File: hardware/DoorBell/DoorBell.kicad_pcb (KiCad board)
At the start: 2 copper layers, 17.8 x 33 mm, 5 parts, among them P1 Digital, P2 COM, P3 ADC, P4 Analog, P5 ADC

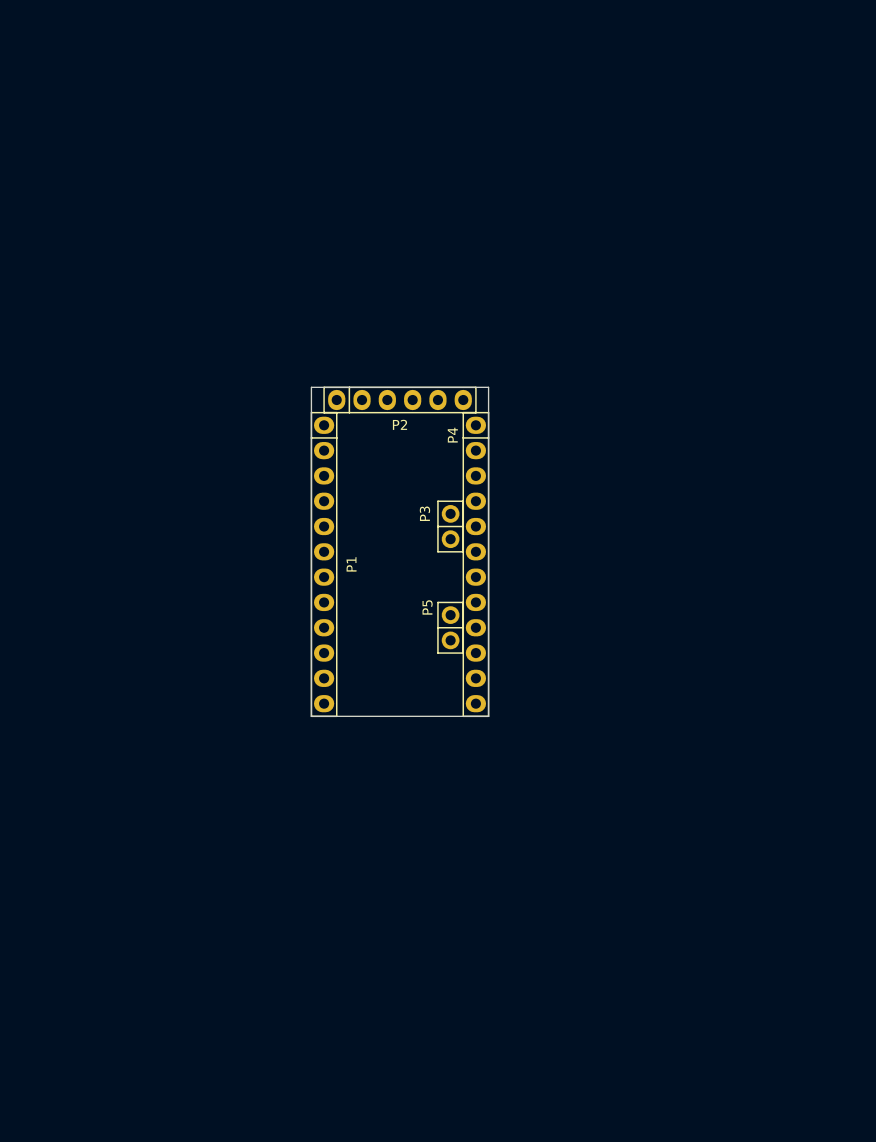
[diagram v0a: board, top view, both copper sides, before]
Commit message: Added mounting holes
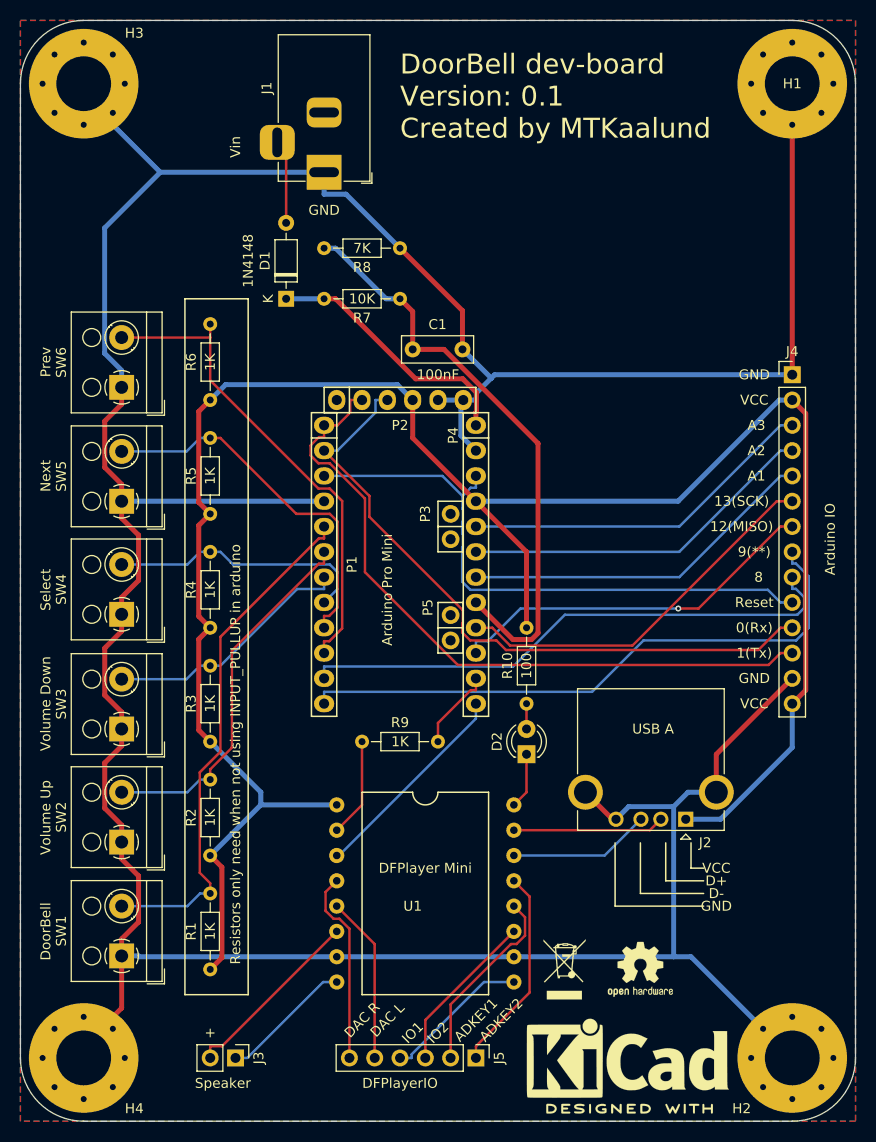
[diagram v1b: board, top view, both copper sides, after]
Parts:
- added C1: 100n, Capacitor_THT:C_Rect_L7.0mm_W2.5mm_P5.00mm, F.Cu at (147.3, 77.5)
- added D1: 1N4148, Diode_THT:D_DO-35_SOD27_P7.62mm_Horizontal, F.Cu at (134.6, 72.4)
- added D2: LED, LED_THT:LED_D3.0mm, F.Cu at (158.8, 118.1)
- added H1: MountingHole_Pad, MountingHole:MountingHole_5.5mm_Pad_Via, F.Cu at (185.4, 50.8)
- added H2: MountingHole_Pad, MountingHole:MountingHole_5.5mm_Pad_Via, F.Cu at (185.4, 148.6)
- added H3: MountingHole_Pad, MountingHole:MountingHole_5.5mm_Pad_Via, F.Cu at (114.3, 50.8)
- added H4: MountingHole_Pad, MountingHole:MountingHole_5.5mm_Pad_Via, F.Cu at (114.3, 148.6)
- added J1: Barrel_Jack_Switch_Pin3Ring, Connector_BarrelJack:BarrelJack_Horizontal, F.Cu at (138.4, 59.7)
- added J2: USB_A, Connector_USB:USB_A_CONNFLY_DS1095-WNR0, F.Cu at (174.7, 124.6)
- added J3: Speaker, Connector_PinHeader_2.54mm:PinHeader_1x02_P2.54mm_Vertical, F.Cu at (129.5, 148.6)
- added J4: ARDUINO_IO, Connector_PinHeader_2.54mm:PinHeader_1x14_P2.54mm_Vertical, F.Cu at (185.4, 80.0)
- added J5: DFPlayerIO, Connector_PinHeader_2.54mm:PinHeader_1x06_P2.54mm_Vertical, F.Cu at (153.7, 148.6)
- added R1: 1K, Resistor_THT:R_Axial_DIN0204_L3.6mm_D1.6mm_P7.62mm_Horizontal, F.Cu at (127.0, 139.7)
- added R10: 100, Resistor_THT:R_Axial_DIN0204_L3.6mm_D1.6mm_P7.62mm_Horizontal, F.Cu at (158.8, 113.0)
- added R2: 1K, Resistor_THT:R_Axial_DIN0204_L3.6mm_D1.6mm_P7.62mm_Horizontal, F.Cu at (127.0, 128.3)
- added R3: 1K, Resistor_THT:R_Axial_DIN0204_L3.6mm_D1.6mm_P7.62mm_Horizontal, F.Cu at (127.0, 116.8)
- added R4: 1K, Resistor_THT:R_Axial_DIN0204_L3.6mm_D1.6mm_P7.62mm_Horizontal, F.Cu at (127.0, 105.4)
- added R5: 1K, Resistor_THT:R_Axial_DIN0204_L3.6mm_D1.6mm_P7.62mm_Horizontal, F.Cu at (127.0, 94.0)
- added R6: 1K, Resistor_THT:R_Axial_DIN0204_L3.6mm_D1.6mm_P7.62mm_Horizontal, F.Cu at (127.0, 82.5)
- added R7: 10K, Resistor_THT:R_Axial_DIN0204_L3.6mm_D1.6mm_P7.62mm_Horizontal, F.Cu at (146.1, 72.4)
- added R8: 7K, Resistor_THT:R_Axial_DIN0204_L3.6mm_D1.6mm_P7.62mm_Horizontal, F.Cu at (146.1, 67.3)
- added R9: 1K, Resistor_THT:R_Axial_DIN0204_L3.6mm_D1.6mm_P7.62mm_Horizontal, F.Cu at (142.2, 116.8)
- added REF**: WEEE-Logo_4.2x6mm_SilkScreen, Symbol:WEEE-Logo_4.2x6mm_SilkScreen, F.Cu at (162.6, 139.7)
- added REF**: OSHW-Logo2_7.3x6mm_SilkScreen, Symbol:OSHW-Logo2_7.3x6mm_SilkScreen, F.Cu at (170.2, 139.7)
- added REF**: KiCad-Logo2_8mm_SilkScreen, Symbol:KiCad-Logo2_8mm_SilkScreen, F.Cu at (168.9, 148.6)
- added SW1: DoorBell, TerminalBlock_RND:TerminalBlock_RND_205-00001_1x02_P5.00mm_Horizontal, F.Cu at (118.1, 138.3)
- added SW2: Volume Up, TerminalBlock_RND:TerminalBlock_RND_205-00001_1x02_P5.00mm_Horizontal, F.Cu at (118.1, 126.9)
- added SW3: Volume Down, TerminalBlock_RND:TerminalBlock_RND_205-00001_1x02_P5.00mm_Horizontal, F.Cu at (118.1, 115.6)
- added SW4: Select, TerminalBlock_RND:TerminalBlock_RND_205-00001_1x02_P5.00mm_Horizontal, F.Cu at (118.1, 104.1)
- added SW5: Next, TerminalBlock_RND:TerminalBlock_RND_205-00001_1x02_P5.00mm_Horizontal, F.Cu at (118.1, 92.7)
- added SW6: Prev, TerminalBlock_RND:TerminalBlock_RND_205-00001_1x02_P5.00mm_Horizontal, F.Cu at (118.1, 81.3)
- added U1: DFPLAYER_MINI, Arduino:DFPlayer_V2, F.Cu at (147.3, 123.2)
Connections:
- P1 pad 10: /7 -> Pin7
- P1 pad 5: /2 -> Pin2
- P1 pad 6: /3(**) -> Pin3
- P1 pad 7: /4 -> Pin4
- P1 pad 8: /5(**) -> Pin5
- P1 pad 9: /6(**) -> Pin6
- P4 pad 1: /RAW -> RAW
- P4 pad 11: /11(**/MOSI) -> DF_RX
- P4 pad 12: /10(**/SS) -> DF_TX
- P4 pad 8: /A0 -> PWR_MON
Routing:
- net GND: track 0.00 -> 458.2 mm
- net VCC: track 0.00 -> 207.6 mm
- net /1(Tx): track 0.00 -> 71.4 mm
- net /0(Rx): track 0.00 -> 68.0 mm
- net /9(**): track 0.00 -> 61.0 mm
- net /Reset: track 0.00 -> 60.3 mm
- net PWR_MON: track 0.00 -> 58.9 mm
- net /8: track 0.00 -> 55.6 mm
- net Pin2: track 0.00 -> 52.2 mm
- net Pin7: track 0.00 -> 49.1 mm
- net /13(SCK): track 0.00 -> 38.5 mm
- net /12(MISO): track 0.00 -> 37.7 mm, vias 0 -> 1
- net Pin3: track 0.00 -> 37.3 mm
- net Pin6: track 0.00 -> 37.2 mm
- net /A2: track 0.00 -> 36.0 mm
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- added copper zone on B.Cu, net GND
- added copper zone on F.Cu, net GND
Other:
- board size 17.8 x 33 mm -> 83.8 x 110.5 mm
- net class Power added: clearance 0.2, trace_width 0.5, via_dia 0.6, via_drill 0.4
- board text added: "+"
- board text added: "0(Rx)"
- board text added: "1(Tx)"
- board text added: "100"
- board text added: "100nF"
- board text added: "10K"
- board text added: "12(MISO)"
- board text added: "13(SCK)"
- board text added: "1K"
- board text added: "1N4148"
- board text added: "7K"
- board text added: "8"
- board text added: "9(**)"
- board text added: "A1"
- board text added: "A2"
- board text added: "A3"
- board text added: "ADKEY1"
- board text added: "ADKEY2"
- board text added: "Arduino IO"
- board text added: "Arduino Pro Mini"
- board text added: "D+"
- board text added: "D-"
- board text added: "DAC L"
- board text added: "DAC R"
- board text added: "DFPlayer Mini"
- board text added: "DFPlayerIO"
- board text added: "DoorBell"
- board text added: "DoorBell dev-board Version: 0.1 Created by MTKaalund"
- board text added: "GND"
- board text added: "IO1"
- board text added: "IO2"
- board text added: "Next"
- board text added: "Prev"
- board text added: "Reset"
- board text added: "Resistors only need when not using INPUT_PULLUP in arduino"
- board text added: "Select"
- board text added: "Speaker"
- board text added: "USB A"
- board text added: "VCC"
- board text added: "Vin"
- board text added: "Volume Down"
- board text added: "Volume Up"
